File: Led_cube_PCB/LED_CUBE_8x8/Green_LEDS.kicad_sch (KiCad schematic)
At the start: 100 parts, among them IC1 74AHCT244PW,118, IC10 74AHCT244PW,118, IC11 74AHCT244PW,118, IC12 74AHCT244PW,118, IC2 74AHCT244PW,118, IC26 SN74HCS238DYYR, IC3 74AHCT244PW,118, IC8 74AHCT244PW,118, IC9 74AHCT244PW,118, J5 Conn_02x16_Odd_Even, J6 Conn_02x16_Odd_Even

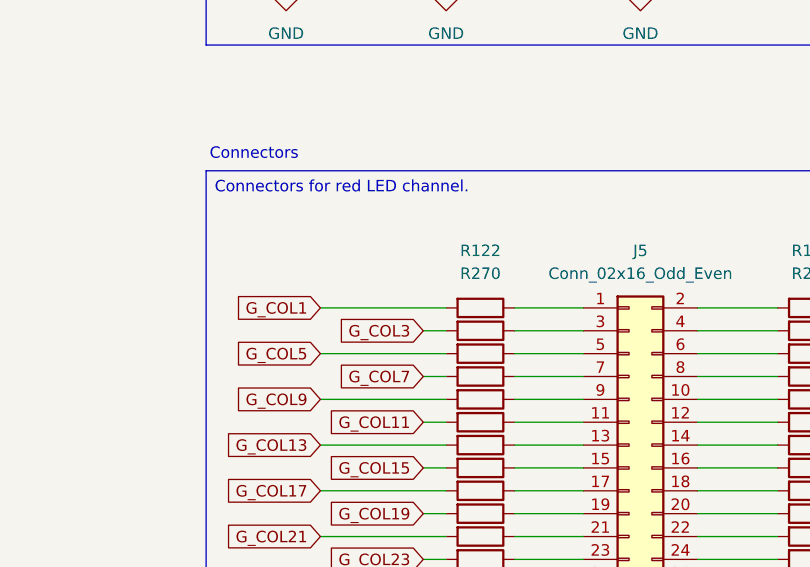
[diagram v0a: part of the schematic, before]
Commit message: Added test points and solder jumpers
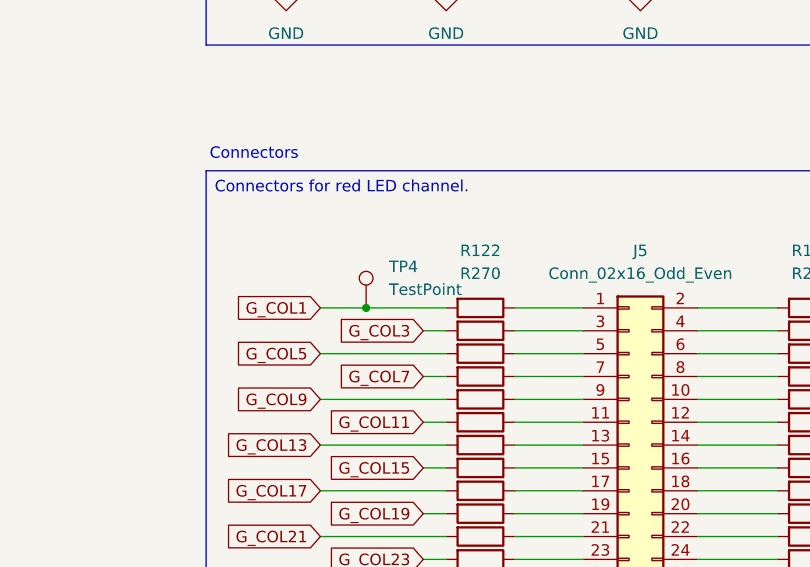
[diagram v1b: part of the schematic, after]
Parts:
- added TP4: TestPoint, TestPoint:TestPoint_Pad_D2.0mm, symbol Connector:TestPoint
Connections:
- net G_COL1: now also TP4.1
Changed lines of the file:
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@@
 	)
 	(junction
+		(at 306.07 83.82)
+		(diameter 0)
+		(color 0 0 0 0)
+	)
+	(junction
 		(at 104.14 91.44)
 		(diameter 0)
@@
 	(wire
 		(pts
+			(xy 306.07 83.82) (xy 314.96 83.82)
+		)
+		(stroke
+			(width 0)
+			(type default)
+		)
+	)
+	(wire
+		(pts
 			(xy 151.13 96.52) (xy 175.26 96.52)
 		)
@@
 	(wire
 		(pts
-			(xy 300.99 83.82) (xy 314.96 83.82)
+			(xy 300.99 83.82) (xy 306.07 83.82)
 		)
 		(stroke
@@
 					(unit 1)
 				)
+			)
+		)
+	)
+	(symbol
+		(lib_id "Connector:TestPoint")
+		(at 306.07 83.82 0)
+		(unit 1)
+		(body_style 1)
+		(exclude_from_sim no)
+		(in_bom yes)
+		(on_board yes)
+		(in_pos_files yes)
+		(dnp no)
+		(fields_autoplaced yes)
+		(property "Reference" "TP4"
+			(at 308.61 79.2479 0)
+			(show_name no)
+			(do_not_autoplace no)
+			(effects
+				(font
+					(size 1.27 1.27)
+				)
+				(justify left)
+			)
+		)
+		(property "Value" "TestPoint"
+			(at 308.61 81.7879 0)
+			(show_name no)
+			(do_not_autoplace no)
+			(effects
+				(font
+					(size 1.27 1.27)
+				)
+				(justify left)
+			)
+		)
+		(property "Footprint" "TestPoint:TestPoint_Pad_D2.0mm"
+			(at 311.15 83.82 0)
+			(hide yes)
+			(show_name no)
+			(do_not_autoplace no)
+			(effects
+				(font
+					(size 1.27 1.27)
+				)
+			)
+		)
+		(property "Datasheet" ""
+			(at 311.15 83.82 0)
+			(hide yes)
+			(show_name no)
+			(do_not_autoplace no)
+			(effects
+				(font
+					(size 1.27 1.27)
+				)
+			)
+		)
+		(property "Description" "test point"
+			(at 306.07 83.82 0)
+			(hide yes)
+			(show_name no)
+			(do_not_autoplace no)
+			(effects
+				(font
+					(size 1.27 1.27)
+				)
+			)
+		)
+		(pin "1"
+		)
+		(instances
+			(project "LED_CUBE_8x8"
+				(path "/b239677e-e361-4439-8200-63fb41f7e03c/028ca277-4d5d-4d09-af7b-5a73ce3cf523"
+					(reference "TP4")
+					(unit 1)
+				)
